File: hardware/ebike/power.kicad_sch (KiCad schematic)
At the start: 26 parts, among them IC1 DRV8302, J1 Screw_Terminal_01x02

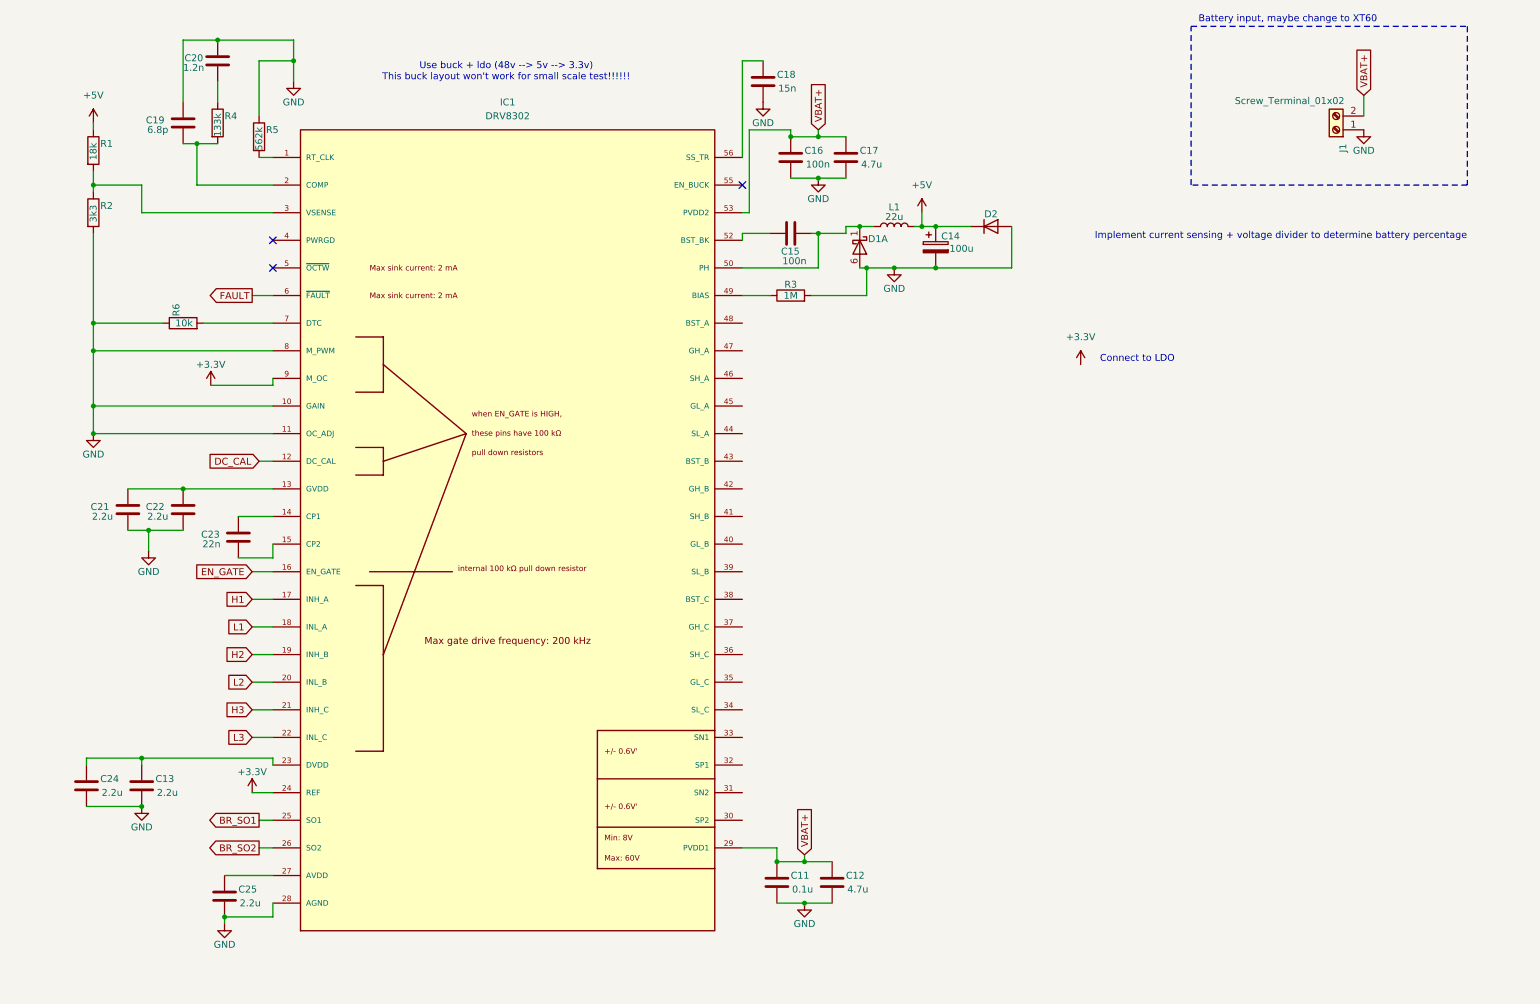
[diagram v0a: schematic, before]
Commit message: first draft of motor control circuitry, need to annotate still
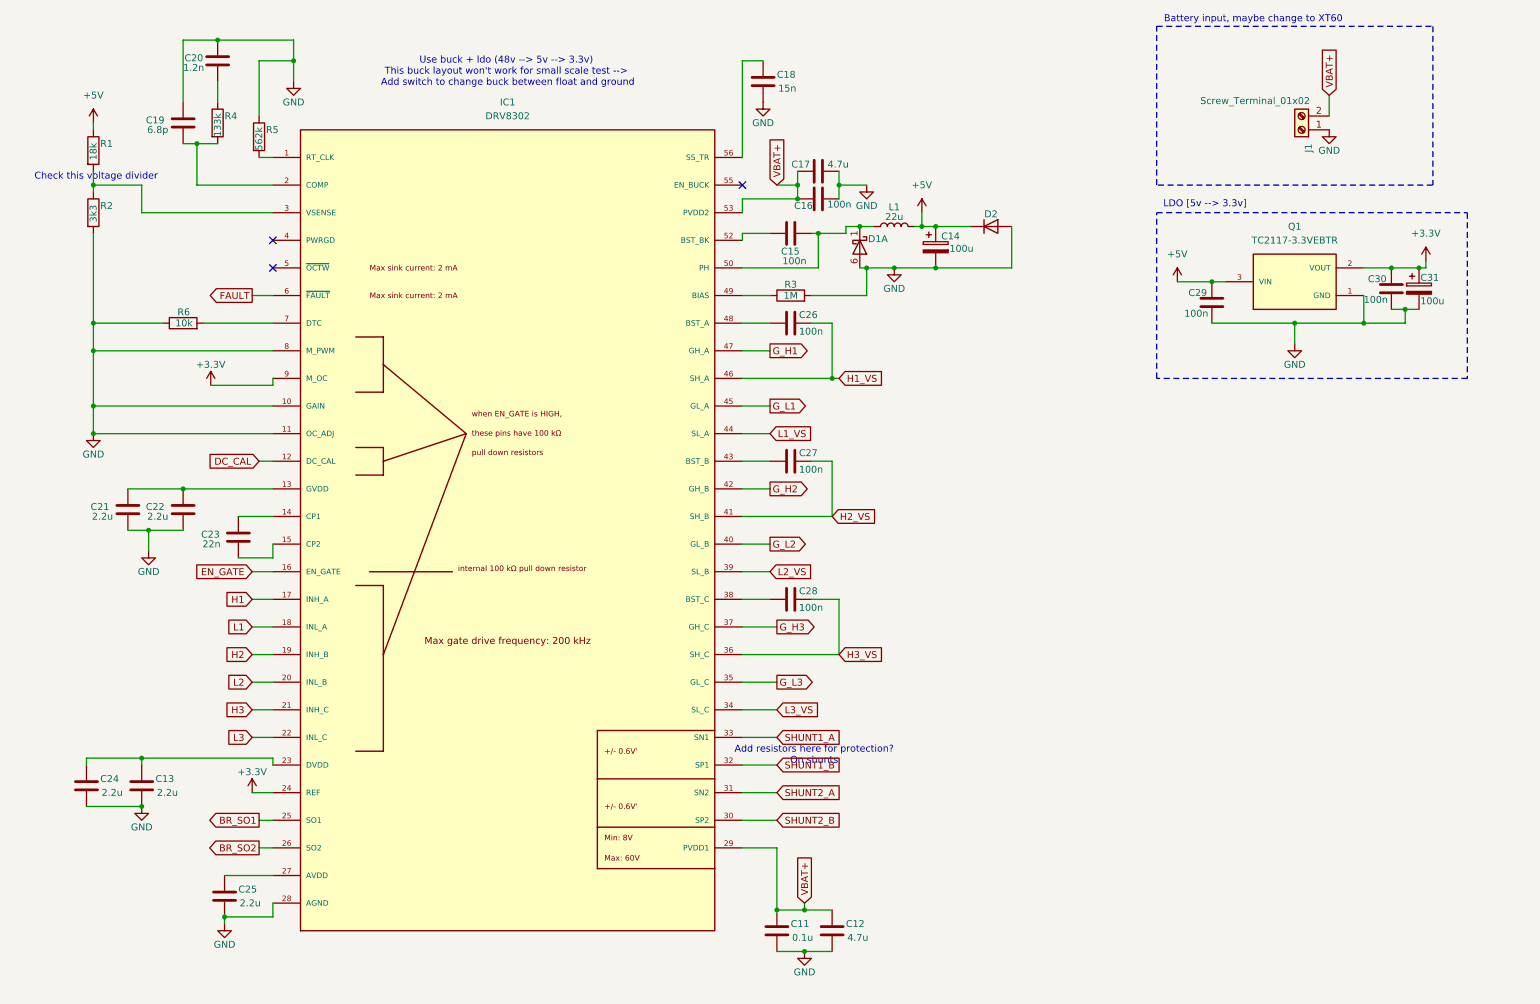
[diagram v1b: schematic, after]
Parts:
- added C26, C27, C28, C29, C30: 100n, symbol Device:C
- added C31: 100u, symbol Device:C_Polarized
- added Q1: TC2117-3.3VEBTR, TC2117-3.3VEBTR:TO254P1491X483-4N, symbol LDO:TC2117-3.3VEBTR
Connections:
- net +3.3V: now also C30.2, C31.1, Q1.2 (VOUT), Q1.4 (VOUT)
- net +5V: now also C29.2, Q1.3 (VIN)
- net AGND: now also C29.1, C30.1, C31.2, Q1.1 (GND)
- net SHUNT2_B: now reaches IC1.30 (SP2)
- net SHUNT2_A: now reaches IC1.31 (SN2)
- net SHUNT1_B: now reaches IC1.32 (SP1)
- net SHUNT1_A: now reaches IC1.33 (SN1)
- net L3_VS: now reaches IC1.34 (SL_C)
- net G_L3: now reaches IC1.35 (GL_C)
- net H3_VS: now reaches IC1.36 (SH_C)
- net H3_VS: now also C28.2
- net G_H3: now reaches IC1.37 (GH_C)
- net at IC1.38 (BST_C): now also C28.1
- net L2_VS: now reaches IC1.39 (SL_B)
- net G_L2: now reaches IC1.40 (GL_B)
- net H2_VS: now reaches IC1.41 (SH_B)
- net H2_VS: now also C27.2
- net G_H2: now reaches IC1.42 (GH_B)
- net at IC1.43 (BST_B): now also C27.1
- net L1_VS: now reaches IC1.44 (SL_A)
- net G_L1: now reaches IC1.45 (GL_A)
- net H1_VS: now reaches IC1.46 (SH_A)
- net H1_VS: now also C26.2
- net G_H1: now reaches IC1.47 (GH_A)
- net at IC1.48 (BST_A): now also C26.1
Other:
- note added: "Add resistors here for protection? On shunts"
- note added: "Check this voltage divider"
- note added: "LDO [5v --> 3.3v]"
- note added: "Use buck + ldo (48v --> 5v --> 3.3v) This buck layout won't work for small scale test --> Add switch to change buck between float and ground"
- note removed: "Connect to LDO"
- note removed: "Implement current sensing + voltage divider to determine battery percentage"
- note removed: "Use buck + ldo (48v --> 5v --> 3.3v) This buck layout won't work for small scale test!!!!!!"
- moved on the sheet: C11, C12, C16, C17, J1

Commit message: Wired PWM, ADC to MCU. Added HAL filtration + battery decoupling
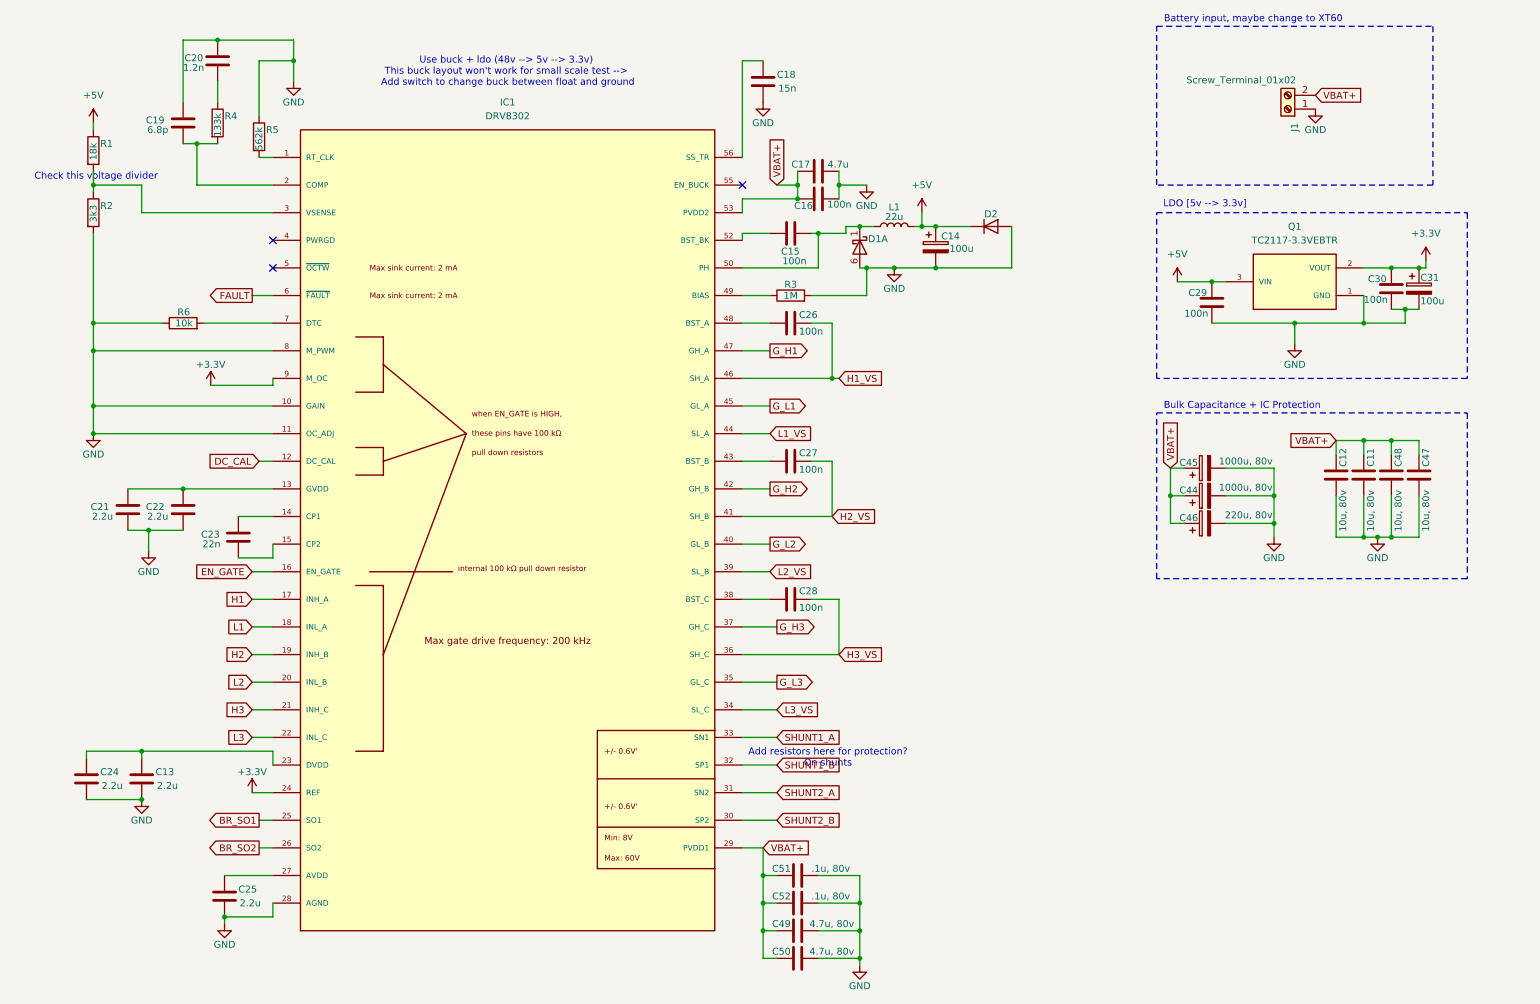
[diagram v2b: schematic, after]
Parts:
- added C44, C45: 1000u, 80v, symbol Device:C_Polarized
- added C46: 220u, 80v, symbol Device:C_Polarized
- added C47, C48: 10u, 80v, symbol Device:C
- added C49, C50: 4.7u, 80v, symbol Device:C
- added C51, C52: .1u, 80v, symbol Device:C
- C11: value 0.1u -> 10u, 80v
- C12: value 4.7u -> 10u, 80v
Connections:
- net AGND: now also C44.2, C45.2, C46.2, C47.2, C48.2, C49.2, C50.2, C51.2, C52.2
- net VBAT+: now also C44.1, C45.1, C46.1, C47.1, C48.1, C49.1, C50.1, C51.1, C52.1
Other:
- note added: "Bulk Capacitance + IC Protection"
- moved on the sheet: C13, C24, J1

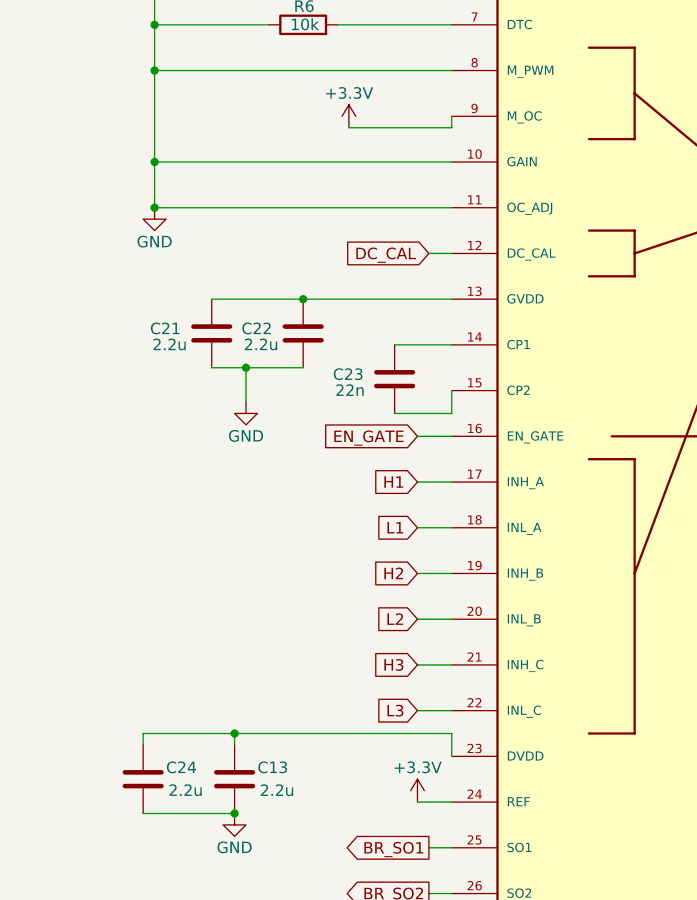
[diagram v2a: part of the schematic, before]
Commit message: wired most of peripherals
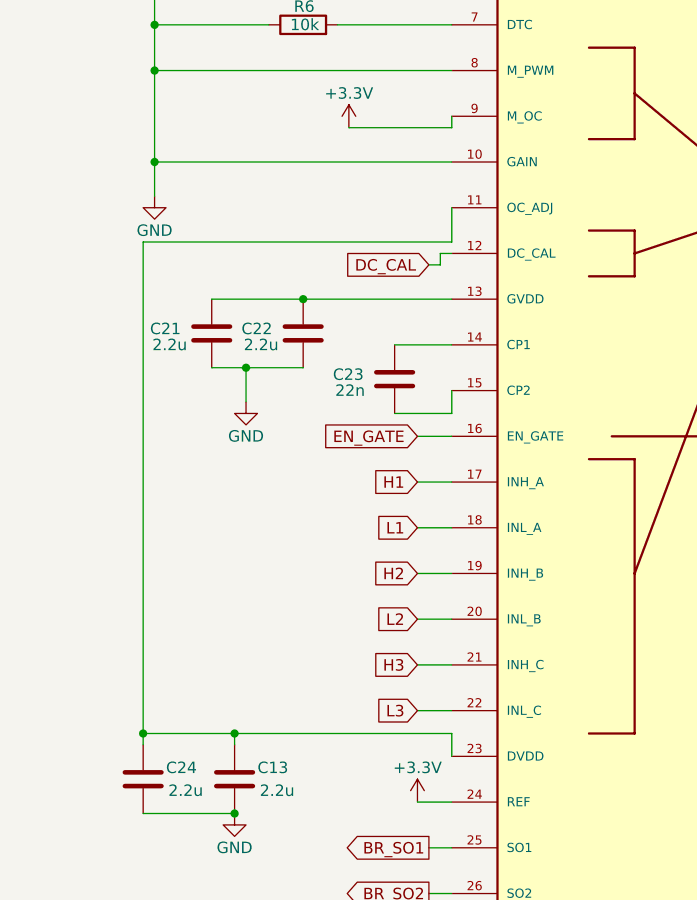
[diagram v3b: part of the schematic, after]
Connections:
- net AGND: no longer IC1.11 (OC_ADJ)
- net at C13.1, C24.1, IC1.23 (DVDD): now also IC1.11 (OC_ADJ)
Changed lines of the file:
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@@
 	)
 	(junction
-		(at 26.67 92.71)
-		(diameter 0)
-		(color 0 0 0 0)
-	)
-	(junction
 		(at 247.65 72.39)
 		(diameter 0)
@@
 	)
 	(junction
+		(at 25.4 151.13)
+		(diameter 0)
+		(color 0 0 0 0)
+	)
+	(junction
 		(at 167.64 189.23)
 		(diameter 0)
@@
 	(wire
 		(pts
+			(xy 25.4 96.52) (xy 59.69 96.52)
+		)
+		(stroke
+			(width 0)
+			(type default)
+		)
+	)
+	(wire
+		(pts
 			(xy 168.91 62.23) (xy 173.99 62.23)
 		)
@@
 	(wire
 		(pts
+			(xy 25.4 151.13) (xy 35.56 151.13)
+		)
+		(stroke
+			(width 0)
+			(type default)
+		)
+	)
+	(wire
+		(pts
 			(xy 33.02 102.87) (xy 43.18 102.87)
 		)
@@
 	(wire
 		(pts
-			(xy 26.67 92.71) (xy 59.69 92.71)
-		)
-		(stroke
-			(width 0)
-			(type default)
-		)
-	)
-	(wire
-		(pts
 			(xy 224.79 99.06) (xy 224.79 104.14)
 		)
@@
 	(wire
 		(pts
-			(xy 25.4 151.13) (xy 35.56 151.13)
-		)
-		(stroke
-			(width 0)
-			(type default)
-		)
-	)
-	(wire
-		(pts
 			(xy 63.5 27.94) (xy 63.5 24.13)
 		)
@@
 	(wire
 		(pts
-			(xy 26.67 92.71) (xy 26.67 87.63)
+			(xy 26.67 91.44) (xy 26.67 87.63)
 		)
 		(stroke
@@
 	(wire
 		(pts
+			(xy 59.69 96.52) (xy 59.69 92.71)
+		)
+		(stroke
+			(width 0)
+			(type default)
+		)
+	)
+	(wire
+		(pts
 			(xy 149.86 168.91) (xy 149.86 173.99)
 		)
@@
 	(wire
 		(pts
+			(xy 58.42 99.06) (xy 58.42 97.79)
+		)
+		(stroke
+			(width 0)
+			(type default)
+		)
+	)
+	(wire
+		(pts
 			(xy 50.8 181.61) (xy 59.69 181.61)
 		)
@@
 	(wire
 		(pts
+			(xy 58.42 97.79) (xy 59.69 97.79)
+		)
+		(stroke
+			(width 0)
+			(type default)
+		)
+	)
+	(wire
+		(pts
 			(xy 160.02 55.88) (xy 165.1 55.88)
 		)
@@
 	(wire
 		(pts
-			(xy 57.15 97.79) (xy 59.69 97.79)
+			(xy 57.15 99.06) (xy 58.42 99.06)
 		)
 		(stroke
@@
 	(wire
 		(pts
+			(xy 25.4 96.52) (xy 25.4 151.13)
+		)
+		(stroke
+			(width 0)
+			(type default)
+		)
+	)
+	(wire
+		(pts
 			(xy 25.4 151.13) (xy 25.4 152.4)
 		)
@@
 	(global_label "DC_CAL"
 		(shape input)
-		(at 57.15 97.79 180)
+		(at 57.15 99.06 180)
 		(fields_autoplaced yes)
 		(effects
@@
 		)
 		(property "Intersheetrefs" "${INTERSHEET_REFS}"
-			(at 47.2705 97.79 0)
+			(at 47.2705 99.06 0)
 			(effects
 				(font
@@
 	(symbol
 		(lib_id "power:GND")
-		(at 26.67 92.71 0)
+		(at 26.67 91.44 0)
 		(unit 1)
 		(exclude_from_sim no)
@@
 		(dnp no)
 		(property "Reference" "#PWR010"
-			(at 26.67 99.06 0)
+			(at 26.67 97.79 0)
 			(effects
 				(font
@@
 		)
 		(property "Value" "GND"
-			(at 26.67 96.52 0)
+			(at 26.67 95.25 0)
 			(effects
 				(font
@@
 		)
 		(property "Footprint" ""
-			(at 26.67 92.71 0)
+			(at 26.67 91.44 0)
 			(effects
 				(font
@@
 		)
 		(property "Datasheet" ""
-			(at 26.67 92.71 0)
+			(at 26.67 91.44 0)
 			(effects
 				(font
@@
 		)
 		(property "Description" "Power symbol creates a global label with name \"GND\" , ground"
-			(at 26.67 92.71 0)
+			(at 26.67 91.44 0)
 			(effects
 				(font
